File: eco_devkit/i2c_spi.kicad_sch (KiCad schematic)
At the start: 24 parts, among them J11 DISPLAY FFC, J12 Micro_SD_Card_Det1, Q3 T2N7002AK,LM, Q4 SL2301S, U3 LTR-329ALS-01, U4 MC3419

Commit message: Notate schematic.
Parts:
- renumbered Q3 to Q5, Q4 to Q6, R42 to R45, R43 to R46, R44 to R47, R45 to R48, R46 to R49, R47 to R50, R48 to R51, R49 to R52
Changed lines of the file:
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@@
 		(dnp no)
 		(fields_autoplaced yes)
-		(property "Reference" "#PWR086"
+		(property "Reference" "#PWR090"
 			(at 139.7 72.39 0)
 			(effects
@@
 			(project "eco_devkit"
 				(path "/308cd3d6-c3d9-49fe-9127-06fda61df52b/18936539-b78a-4a13-b6a3-f93843840718"
-					(reference "#PWR086")
+					(reference "#PWR090")
 					(unit 1)
 				)
@@
 		(dnp no)
 		(fields_autoplaced yes)
-		(property "Reference" "#PWR081"
+		(property "Reference" "#PWR085"
 			(at 83.82 146.05 0)
 			(effects
@@
 			(project "eco_devkit"
 				(path "/308cd3d6-c3d9-49fe-9127-06fda61df52b/18936539-b78a-4a13-b6a3-f93843840718"
-					(reference "#PWR081")
+					(reference "#PWR085")
 					(unit 1)
 				)
@@
 		(dnp no)
 		(fields_autoplaced yes)
-		(property "Reference" "#PWR089"
+		(property "Reference" "#PWR093"
 			(at 166.37 72.39 0)
 			(effects
@@
 			(project "eco_devkit"
 				(path "/308cd3d6-c3d9-49fe-9127-06fda61df52b/18936539-b78a-4a13-b6a3-f93843840718"
-					(reference "#PWR089")
+					(reference "#PWR093")
 					(unit 1)
 				)
@@
 		(dnp no)
 		(fields_autoplaced yes)
-		(property "Reference" "#PWR082"
+		(property "Reference" "#PWR086"
 			(at 83.82 175.26 0)
 			(effects
@@
 			(project "eco_devkit"
 				(path "/308cd3d6-c3d9-49fe-9127-06fda61df52b/18936539-b78a-4a13-b6a3-f93843840718"
-					(reference "#PWR082")
+					(reference "#PWR086")
 					(unit 1)
 				)
@@
 		(dnp no)
 		(fields_autoplaced yes)
-		(property "Reference" "R49"
+		(property "Reference" "R52"
 			(at 214.63 60.9599 0)
 			(effects
@@
 			(project "eco_devkit"
 				(path "/308cd3d6-c3d9-49fe-9127-06fda61df52b/18936539-b78a-4a13-b6a3-f93843840718"
-					(reference "R49")
+					(reference "R52")
 					(unit 1)
 				)
@@
 		(dnp no)
 		(fields_autoplaced yes)
-		(property "Reference" "#PWR076"
+		(property "Reference" "#PWR080"
 			(at 43.18 73.66 0)
 			(effects
@@
 			(project "eco_devkit"
 				(path "/308cd3d6-c3d9-49fe-9127-06fda61df52b/18936539-b78a-4a13-b6a3-f93843840718"
-					(reference "#PWR076")
+					(reference "#PWR080")
 					(unit 1)
 				)
@@
 		(dnp no)
 		(fields_autoplaced yes)
-		(property "Reference" "R45"
+		(property "Reference" "R48"
 			(at 147.32 146.0499 0)
 			(effects
@@
 			(project "eco_devkit"
 				(path "/308cd3d6-c3d9-49fe-9127-06fda61df52b/18936539-b78a-4a13-b6a3-f93843840718"
-					(reference "R45")
+					(reference "R48")
 					(unit 1)
 				)
@@
 		(dnp no)
 		(fields_autoplaced yes)
-		(property "Reference" "R47"
+		(property "Reference" "R50"
 			(at 147.32 96.52 90)
 			(effects
@@
 			(project "eco_devkit"
 				(path "/308cd3d6-c3d9-49fe-9127-06fda61df52b/18936539-b78a-4a13-b6a3-f93843840718"
-					(reference "R47")
+					(reference "R50")
 					(unit 1)
 				)
@@
 		(dnp no)
 		(fields_autoplaced yes)
-		(property "Reference" "#PWR093"
+		(property "Reference" "#PWR097"
 			(at 265.43 110.49 0)
 			(effects
@@
 			(project "eco_devkit"
 				(path "/308cd3d6-c3d9-49fe-9127-06fda61df52b/18936539-b78a-4a13-b6a3-f93843840718"
-					(reference "#PWR093")
+					(reference "#PWR097")
 					(unit 1)
 				)
@@
 		(dnp no)
 		(fields_autoplaced yes)
-		(property "Reference" "#PWR075"
+		(property "Reference" "#PWR079"
 			(at 34.29 73.66 0)
 			(effects
@@
 			(project "eco_devkit"
 				(path "/308cd3d6-c3d9-49fe-9127-06fda61df52b/18936539-b78a-4a13-b6a3-f93843840718"
-					(reference "#PWR075")
+					(reference "#PWR079")
 					(unit 1)
 				)
@@
 		(dnp no)
 		(fields_autoplaced yes)
-		(property "Reference" "#PWR088"
+		(property "Reference" "#PWR092"
 			(at 153.67 111.76 0)
 			(effects
@@
 			(project ""
 				(path "/308cd3d6-c3d9-49fe-9127-06fda61df52b/18936539-b78a-4a13-b6a3-f93843840718"
-					(reference "#PWR088")
+					(reference "#PWR092")
 					(unit 1)
 				)
@@
 		(on_board yes)
 		(dnp no)
-		(property "Reference" "Q3"
+		(property "Reference" "Q5"
 			(at 157.48 91.4399 0)
 			(effects
@@
 			(project ""
 				(path "/308cd3d6-c3d9-49fe-9127-06fda61df52b/18936539-b78a-4a13-b6a3-f93843840718"
-					(reference "Q3")
+					(reference "Q5")
 					(unit 1)
 				)
@@
 		(dnp no)
 		(fields_autoplaced yes)
-		(property "Reference" "#PWR091"
+		(property "Reference" "#PWR095"
 			(at 208.28 109.22 0)
 			(effects
@@
 			(project "eco_devkit"
 				(path "/308cd3d6-c3d9-49fe-9127-06fda61df52b/18936539-b78a-4a13-b6a3-f93843840718"
-					(reference "#PWR091")
+					(reference "#PWR095")
 					(unit 1)
 				)
@@
 		(dnp no)
 		(fields_autoplaced yes)
-		(property "Reference" "R42"
+		(property "Reference" "R45"
 			(at 36.83 73.6599 0)
 			(effects
@@
 			(project "eco_devkit"
 				(path "/308cd3d6-c3d9-49fe-9127-06fda61df52b/18936539-b78a-4a13-b6a3-f93843840718"
-					(reference "R42")
+					(reference "R45")
 					(unit 1)
 				)
@@
 		(on_board yes)
 		(dnp no)
-		(property "Reference" "Q4"
+		(property "Reference" "Q6"
 			(at 153.67 64.77 90)
 			(effects
@@
 			(project ""
 				(path "/308cd3d6-c3d9-49fe-9127-06fda61df52b/18936539-b78a-4a13-b6a3-f93843840718"
-					(reference "Q4")
+					(reference "Q6")
 					(unit 1)
 				)
@@
 		(dnp no)
 		(fields_autoplaced yes)
-		(property "Reference" "#PWR079"
+		(property "Reference" "#PWR083"
 			(at 68.58 158.75 0)
 			(effects
@@
 			(project "eco_devkit"
 				(path "/308cd3d6-c3d9-49fe-9127-06fda61df52b/18936539-b78a-4a13-b6a3-f93843840718"
-					(reference "#PWR079")
+					(reference "#PWR083")
 					(unit 1)
 				)
@@
 		(dnp no)
 		(fields_autoplaced yes)
-		(property "Reference" "#PWR087"
+		(property "Reference" "#PWR091"
 			(at 144.78 146.05 0)
 			(effects
@@
 			(project "eco_devkit"
 				(path "/308cd3d6-c3d9-49fe-9127-06fda61df52b/18936539-b78a-4a13-b6a3-f93843840718"
-					(reference "#PWR087")
+					(reference "#PWR091")
 					(unit 1)
 				)
@@
 		(dnp no)
 		(fields_autoplaced yes)
-		(property "Reference" "#PWR078"
+		(property "Reference" "#PWR082"
 			(at 68.58 144.78 0)
 			(effects
@@
 			(project "eco_devkit"
 				(path "/308cd3d6-c3d9-49fe-9127-06fda61df52b/18936539-b78a-4a13-b6a3-f93843840718"
-					(reference "#PWR078")
+					(reference "#PWR082")
 					(unit 1)
 				)
@@
 		(dnp no)
 		(fields_autoplaced yes)
-		(property "Reference" "R44"
+		(property "Reference" "R47"
 			(at 137.16 146.0499 0)
 			(effects
@@
 			(project "eco_devkit"
 				(path "/308cd3d6-c3d9-49fe-9127-06fda61df52b/18936539-b78a-4a13-b6a3-f93843840718"
-					(reference "R44")
+					(reference "R47")
 					(unit 1)
 				)
@@
 		(dnp no)
 		(fields_autoplaced yes)
-		(property "Reference" "#PWR077"
+		(property "Reference" "#PWR081"
 			(at 52.07 85.09 0)
 			(effects
@@
 			(project "eco_devkit"
 				(path "/308cd3d6-c3d9-49fe-9127-06fda61df52b/18936539-b78a-4a13-b6a3-f93843840718"
-					(reference "#PWR077")
+					(reference "#PWR081")
 					(unit 1)
 				)
@@
 		(dnp no)
 		(fields_autoplaced yes)
-		(property "Reference" "#PWR085"
+		(property "Reference" "#PWR089"
 			(at 134.62 146.05 0)
 			(effects
@@
 			(project "eco_devkit"
 				(path "/308cd3d6-c3d9-49fe-9127-06fda61df52b/18936539-b78a-4a13-b6a3-f93843840718"
-					(reference "#PWR085")
+					(reference "#PWR089")
 					(unit 1)
 				)
@@
 		(on_board yes)
 		(dnp no)
-		(property "Reference" "R43"
+		(property "Reference" "R46"
 			(at 118.11 60.96 90)
 			(effects
@@
 			(project "eco_devkit"
 				(path "/308cd3d6-c3d9-49fe-9127-06fda61df52b/18936539-b78a-4a13-b6a3-f93843840718"
-					(reference "R43")
+					(reference "R46")
 					(unit 1)
 				)
@@
 		(dnp no)
 		(fields_autoplaced yes)
-		(property "Reference" "#PWR083"
+		(property "Reference" "#PWR087"
 			(at 111.76 113.03 0)
 			(effects
@@
 			(project ""
 				(path "/308cd3d6-c3d9-49fe-9127-06fda61df52b/18936539-b78a-4a13-b6a3-f93843840718"
-					(reference "#PWR083")
+					(reference "#PWR087")
 					(unit 1)
 				)
@@
 		(dnp no)
 		(fields_autoplaced yes)
-		(property "Reference" "R48"
+		(property "Reference" "R51"
 			(at 200.66 60.9599 0)
 			(effects
@@
 			(project "eco_devkit"
 				(path "/308cd3d6-c3d9-49fe-9127-06fda61df52b/18936539-b78a-4a13-b6a3-f93843840718"
-					(reference "R48")
+					(reference "R51")
 					(unit 1)
 				)
@@
 		(dnp no)
 		(fields_autoplaced yes)
-		(property "Reference" "R46"
+		(property "Reference" "R49"
 			(at 147.32 77.47 90)
 			(effects
@@
 			(project "eco_devkit"
 				(path "/308cd3d6-c3d9-49fe-9127-06fda61df52b/18936539-b78a-4a13-b6a3-f93843840718"
-					(reference "R46")
+					(reference "R49")
 					(unit 1)
 				)
@@
 		(dnp no)
 		(fields_autoplaced yes)
-		(property "Reference" "#PWR080"
+		(property "Reference" "#PWR084"
 			(at 78.74 113.03 0)
 			(effects
@@
 			(project "eco_devkit"
 				(path "/308cd3d6-c3d9-49fe-9127-06fda61df52b/18936539-b78a-4a13-b6a3-f93843840718"
-					(reference "#PWR080")
+					(reference "#PWR084")
 					(unit 1)
 				)
@@
 		(dnp no)
 		(fields_autoplaced yes)
-		(property "Reference" "#PWR090"
+		(property "Reference" "#PWR094"
 			(at 198.12 59.69 0)
 			(effects
@@
 			(project "eco_devkit"
 				(path "/308cd3d6-c3d9-49fe-9127-06fda61df52b/18936539-b78a-4a13-b6a3-f93843840718"
-					(reference "#PWR090")
+					(reference "#PWR094")
 					(unit 1)
 				)
@@
 		(dnp no)
 		(fields_autoplaced yes)
-		(property "Reference" "#PWR092"
+		(property "Reference" "#PWR096"
 			(at 212.09 59.69 0)
 			(effects
@@
 			(project "eco_devkit"
 				(path "/308cd3d6-c3d9-49fe-9127-06fda61df52b/18936539-b78a-4a13-b6a3-f93843840718"
-					(reference "#PWR092")
+					(reference "#PWR096")
 					(unit 1)
 				)
@@
 		(dnp no)
 		(fields_autoplaced yes)
-		(property "Reference" "#PWR084"
+		(property "Reference" "#PWR088"
 			(at 132.08 72.39 0)
 			(effects
@@
 			(project "eco_devkit"
 				(path "/308cd3d6-c3d9-49fe-9127-06fda61df52b/18936539-b78a-4a13-b6a3-f93843840718"
-					(reference "#PWR084")
+					(reference "#PWR088")
 					(unit 1)
 				)

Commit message: att
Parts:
- removed C42, C43, C44, C45, C46: 1u, Capacitor_SMD:C_0402_1005Metric, symbol Device:C_Small
- removed C48, C49: 2.2u, Capacitor_SMD:C_0402_1005Metric, symbol Device:C_Small
- removed J11: DISPLAY FFC, Connector_FFC-FPC:Amphenol_F32R-1A7x1-11016_1x16-1MP_P0.5mm_Horizontal, symbol peripherals2:DISPLAY_CONN
- removed Q5: T2N7002AK,LM, symbol Simulation_SPICE:PMOS
- removed Q6: SL2301S, symbol Transistor_FET:Q_NMOS_GDS
- removed R45, R49, R50: 10k, symbol Device:R_Small_US
- removed R46: 560k, symbol Device:R_Small_US
- added C51, C52, C63, C64: 2.2u, Capacitor_SMD:C_0402_1005Metric, symbol Device:C_Small
- added C53, C54, C55, C56, C57, C58, C59, C60, C61, C62: 1u, Capacitor_SMD:C_0402_1005Metric, symbol Device:C_Small
- added J13: ~, symbol peripherals2:DISPLAY_CONN
- added J14: DISPLAY FFC, Connector_FFC-FPC:Amphenol_F32R-1A7x1-11016_1x16-1MP_P0.5mm_Horizontal, symbol peripherals2:DISPLAY_CONN
- added Q10, Q8: SL2301S, symbol Transistor_FET:Q_NMOS_GDS
- added Q7, Q9: T2N7002AK,LM, symbol Simulation_SPICE:PMOS
- added R53, R58: 560k, symbol Device:R_Small_US
- added R54, R55, R56, R57, R59, R60: 10k, symbol Device:R_Small_US
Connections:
- net +3V3: now also C56.1, C57.1, C59.1, C60.1, J13.10 (BS0), J13.9 (VDD), J14.10 (BS0), J14.9 (VDD), Q10.3 (S), Q8.3 (S), R54.1, R56.1, R57.1, R59.1
- net +VDISP: now also C55.1, C58.1, J13.6 (VDDB), J14.6 (VDDB), Q10.2 (D), Q8.2 (D)
- net DISPLAY_CS: now also J13.13 (~{CS}), J14.13 (~{CS})
- net DISPLAY_EN: now also Q7.2 (G), Q9.2 (G), R55.1, R60.1
- net DISPLAY_MOSI: now also J13.19 (D1), J14.19 (D1)
- net DISPLAY_RST: now also J13.14 (~{RES}), J14.14 (~{RES}), R56.2, R57.2
- net DISPLAY_SCK: now also J13.18 (D0), J14.18 (D0)
- net GND: now also C51.1, C52.1, C55.2, C56.2, C57.2, C58.2, C59.2, C60.2, C63.1, C64.1, J13.1 (NC/GND), J13.11 (BS1), J13.15 (~{D/C}), J13.16 (R/~{W}), J13.17 (~{E/RD}), J13.21 (D3), J13.22 (D4), J13.23 (D5), J13.24 (D6), J13.25 (D7), J13.29 (VLSS), J13.30 (GND), J13.8 (VSS), J14.1 (NC/GND), J14.11 (BS1), J14.15 (~{D/C}), J14.16 (R/~{W}), J14.17 (~{E/RD}), J14.21 (D3), J14.22 (D4), J14.23 (D5), J14.24 (D6), J14.25 (D7), J14.29 (VLSS), J14.30 (GND), J14.8 (VSS), Q7.3 (S), Q9.3 (S), R53.1, R55.2, R58.1, R60.2
- new net: C51.2, J13.28 (VCC)
- new net: C54.1, J13.5 (C1N)
- new net: C54.2, J13.4 (C1P)
- new net: C61.1, J14.3 (C2N)
- new net: C61.2, J14.2 (C2P)
- new net: C62.1, J14.5 (C1N)
- new net: C62.2, J14.4 (C1P)
- new net: Q10.1 (G), Q9.1 (D), R59.2
- new net: Q7.1 (D), Q8.1 (G), R54.2
- new net: J14.26 (IREF), R58.2
- new net: C53.1, J13.3 (C2N)
- new net: C53.2, J13.2 (C2P)
- new net: C63.2, J14.28 (VCC)
- new net: J13.26 (IREF), R53.2
- new net: C52.2, J13.27 (VCOMH)
- new net: C64.2, J14.27 (VCOMH)
- no-connect marks 7 -> 9
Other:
- moved on the sheet: C50, J12, JP1, R51, R52

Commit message: chore: Ajuste dos resistores de pull-up para Not Fitted e reorganização dos pinos do display
- Atualizados os resistores de pull-up para status Not Fitted, considerando a possibilidade de uso de pull-ups internos do microcontrolador.
- Reorganizados os pinos do display para que fiquem todos de um único lado, facilitando o roteamento da PCB.
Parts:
- removed C58, C59, C60, C61, C62: 1u, Capacitor_SMD:C_0402_1005Metric, symbol Device:C_Small
- removed C63, C64: 2.2u, Capacitor_SMD:C_0402_1005Metric, symbol Device:C_Small
- removed J14: DISPLAY FFC, Connector_FFC-FPC:Amphenol_F32R-1A7x1-11016_1x16-1MP_P0.5mm_Horizontal, symbol peripherals2:DISPLAY_CONN
- removed Q10: SL2301S, symbol Transistor_FET:Q_NMOS_GDS
- removed Q9: T2N7002AK,LM, symbol Simulation_SPICE:PMOS
- removed R57, R59, R60: 10k, symbol Device:R_Small_US
- removed R58: 560k, symbol Device:R_Small_US
- J13: value ~ -> MCOT064032A1V-YI
- R47, R48, R51, R52: now not fitted
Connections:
- no-connect marks 9 -> 7
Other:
- moved on the sheet: C51, C52, R53

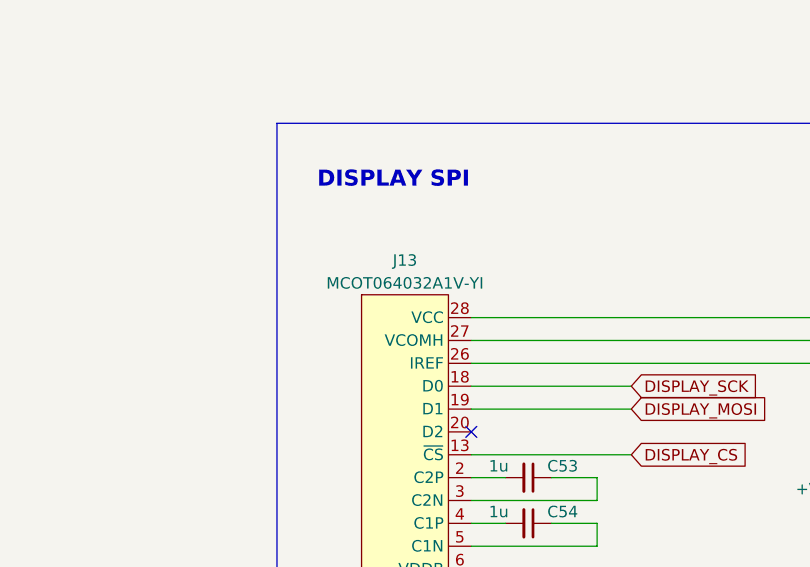
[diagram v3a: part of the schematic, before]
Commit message: feat: ajustes de footprints e revisão de dimensões dos componentes
- Confirmado footprint do slot de cartão SD.
- Adicionado footprint para o sensor de luminosidade I2C (light sensor).
- Adicionado footprint para o display SPI (conector FFC de 28 pinos).
- Revisado e conferido as dimensões dos pads do acelerômetro (ACCEL), validando tamanho de cada área de contato.
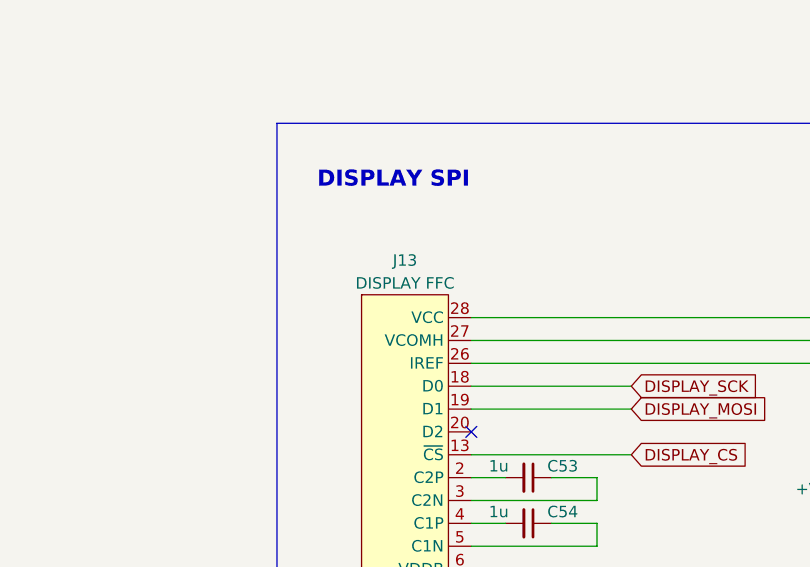
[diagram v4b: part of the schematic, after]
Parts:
- J13: value MCOT064032A1V-YI -> DISPLAY FFC; footprint (none) -> EcoDevkit:AMPHENOL_SFV28R-2STE1HLF; MPN (none) -> CF4228FH0R0-05-NH
- Q7, Q8: footprint (none) -> Package_TO_SOT_SMD:SOT-23
- U3: footprint (none) -> EcoDevkit:LTR-329ALS-01_LTO
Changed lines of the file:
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@@
 			)
 		)
-		(property "Footprint" ""
+		(property "Footprint" "Package_TO_SOT_SMD:SOT-23"
 			(at 262.89 119.38 0)
 			(effects
@@
 			)
 		)
-		(property "Footprint" ""
+		(property "Footprint" "EcoDevkit:LTR-329ALS-01_LTO"
 			(at 52.07 157.48 0)
 			(effects
@@
 			)
 		)
-		(property "Footprint" ""
+		(property "Footprint" "Package_TO_SOT_SMD:SOT-23"
 			(at 262.89 140.97 0)
 			(effects
@@
 			)
 		)
-		(property "Value" "MCOT064032A1V-YI"
+		(property "Value" "DISPLAY FFC"
 			(at 186.944 58.42 0)
 			(effects
@@
 			)
 		)
-		(property "Footprint" ""
+		(property "Footprint" "EcoDevkit:AMPHENOL_SFV28R-2STE1HLF"
 			(at 184.15 78.74 0)
 			(effects
@@
 			)
 		)
-		(property "Datasheet" "https://www.digikey.com.br/pt/products/detail/midas-displays/MCOT064032A1V-YI/21322647"
+		(property "Datasheet" "https://www.digikey.com.br/pt/products/detail/cvilux-usa/CF4228FH0R0-05-NH/15793186"
 			(at 184.15 78.74 0)
 			(effects
@@
 			)
 		)
-		(property "Description" "GRAPHIC DISPLAY OLED YELLOW 0.49"
+		(property "Description" "CONN FFC FPC 28POS 0.5MM R/A"
 			(at 184.15 78.74 0)
 			(effects
+				(font
+					(size 1.27 1.27)
+				)
+				(hide yes)
+			)
+		)
+		(property "MPN" "CF4228FH0R0-05-NH"
+			(at 184.15 78.74 0)
+			(effects
